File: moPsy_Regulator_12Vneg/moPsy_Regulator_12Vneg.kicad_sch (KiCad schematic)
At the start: 14 parts

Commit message: Add 100n cap to the -12V regulator output for stability
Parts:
- added C4: 100n, symbol Device:C
- C1: value (none) -> 10u; footprint (none) -> Capacitor_THT:CP_Radial_D5.0mm_P2.50mm
- C2: value (none) -> 25u; footprint (none) -> Capacitor_THT:CP_Radial_D5.0mm_P2.00mm
- C3: value (none) -> 150u; footprint (none) -> Capacitor_THT:CP_Radial_D8.0mm_P3.50mm
- D1: value (none) -> rt; footprint (none) -> LED_THT:LED_D5.0mm
- J1, J2, J3, J4: value (none) -> Conn_01x01_Male; footprint (none) -> moPsy:Connector FS-P475
- R1: value (none) -> 4k3; footprint (none) -> Resistor_THT:R_Axial_DIN0207_L6.3mm_D2.5mm_P7.62mm_Horizontal
- R2: value (none) -> 2k37; footprint (none) -> Resistor_THT:R_Axial_DIN0207_L6.3mm_D2.5mm_P7.62mm_Horizontal
- R3: value (none) -> 9k1; footprint (none) -> Resistor_THT:R_Axial_DIN0207_L6.3mm_D2.5mm_P7.62mm_Horizontal
- R4: value (none) -> 480R; footprint (none) -> Resistor_THT:R_Axial_DIN0207_L6.3mm_D2.5mm_P2.54mm_Vertical
- RV1: value (none) -> 1k; footprint (none) -> moPsy:Suntan 3296 Trim Pot
- U1: value (none) -> LT1185; footprint (none) -> Package_TO_SOT_THT:TO-220-5_P3.4x3.7mm_StaggerOdd_Lead3.8mm_Vertical
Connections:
- net -12V: now also C4.2
- net GND: now also C4.1
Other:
- moved on the sheet: C3, D1, J3, J4, R4

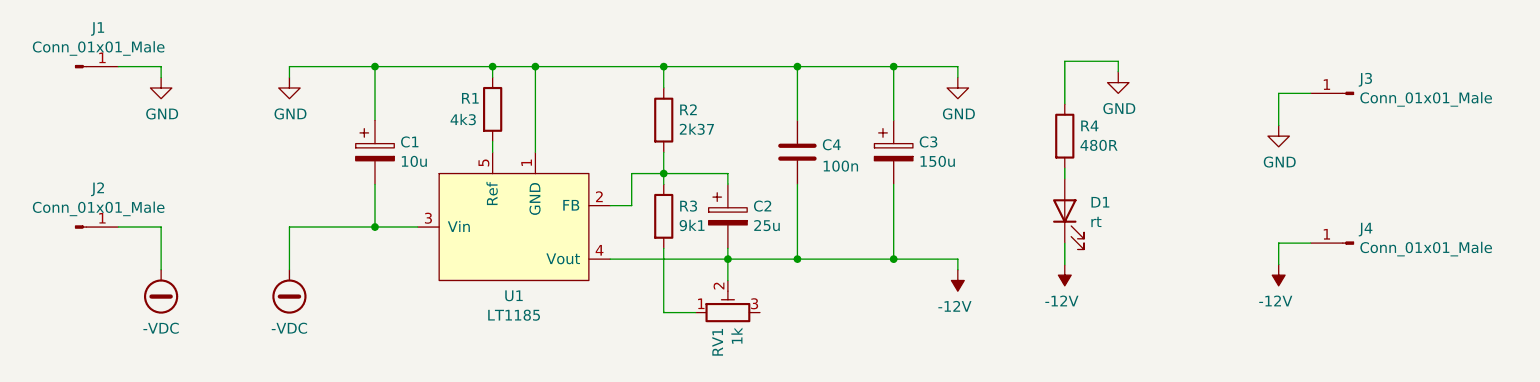
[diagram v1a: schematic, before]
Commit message: Put cap for -12V regulator on PCB
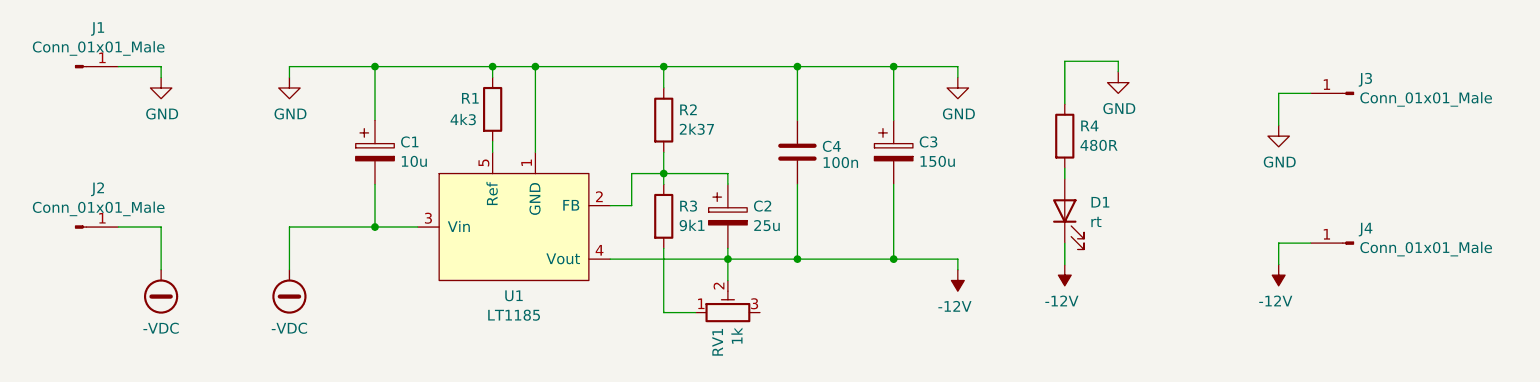
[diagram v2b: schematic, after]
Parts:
- C4: footprint (none) -> Capacitor_THT:C_Rect_L7.0mm_W2.0mm_P5.00mm
